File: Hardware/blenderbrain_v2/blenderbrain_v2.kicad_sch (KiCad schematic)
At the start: 49 parts, among them J1 OxySens2, J2 HeSens1, J24V1 Screw_Terminal_01x02, J3 HeSens2, J4 OxySens1, J5 Conn_01x04_Female, J5V1 Screw_Terminal_01x02, J6 AVR-ISP-6, Q1 IRFR4105, Q2 IRFR4105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

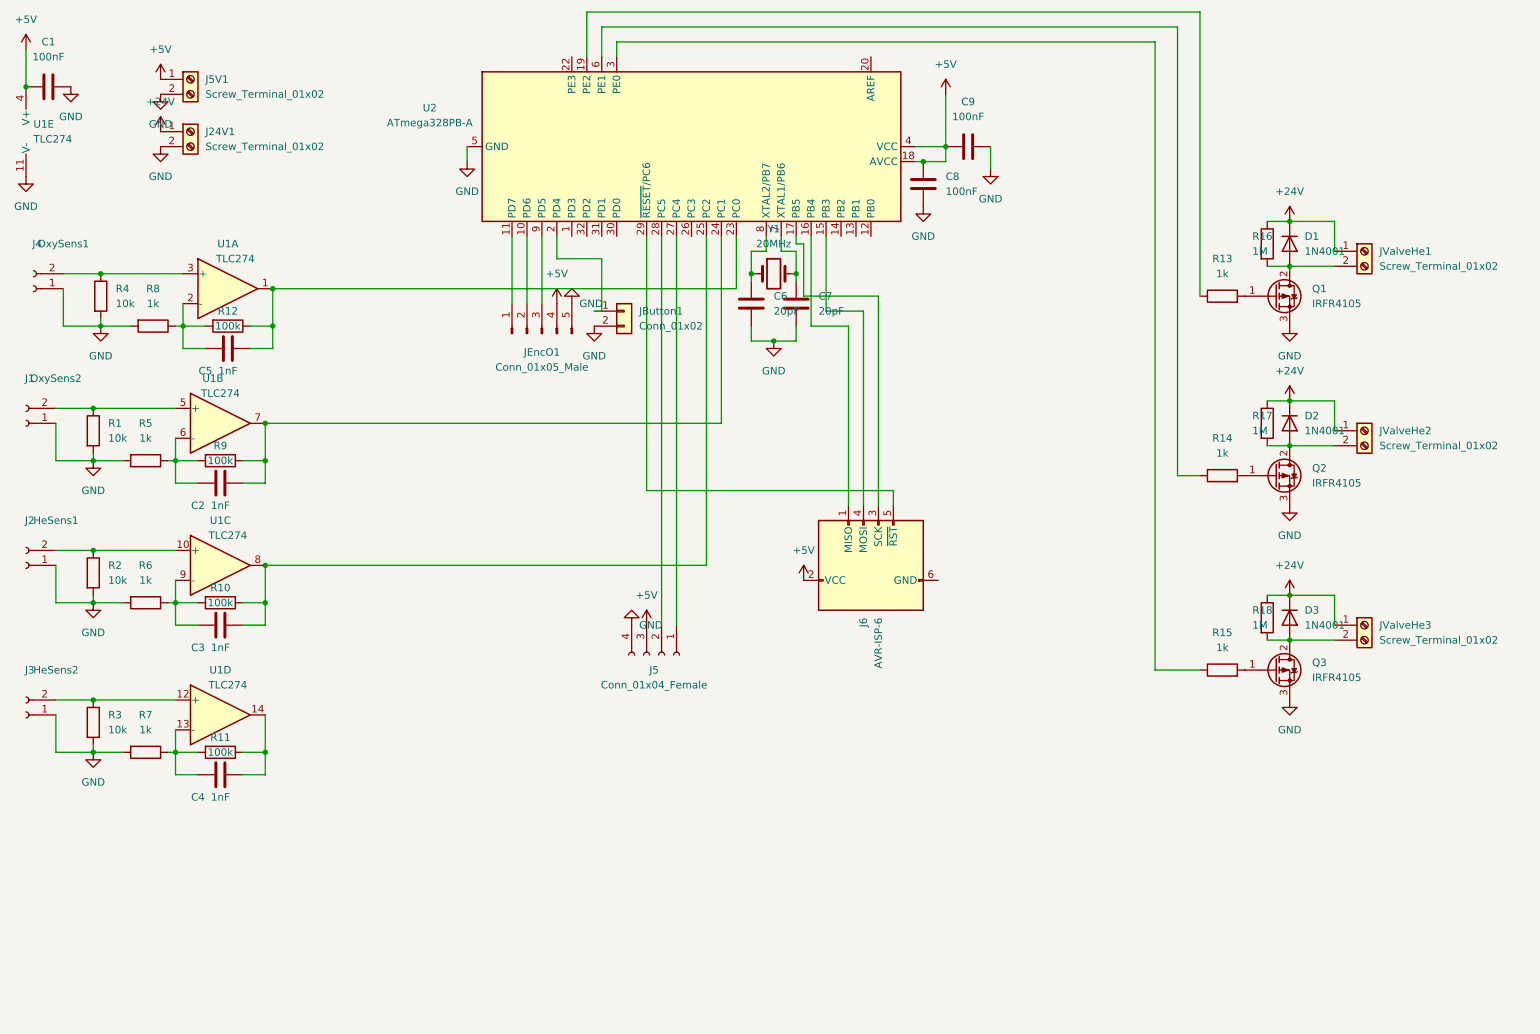
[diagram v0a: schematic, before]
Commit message: hardware: added rotary encoder to pcb and made first alignment
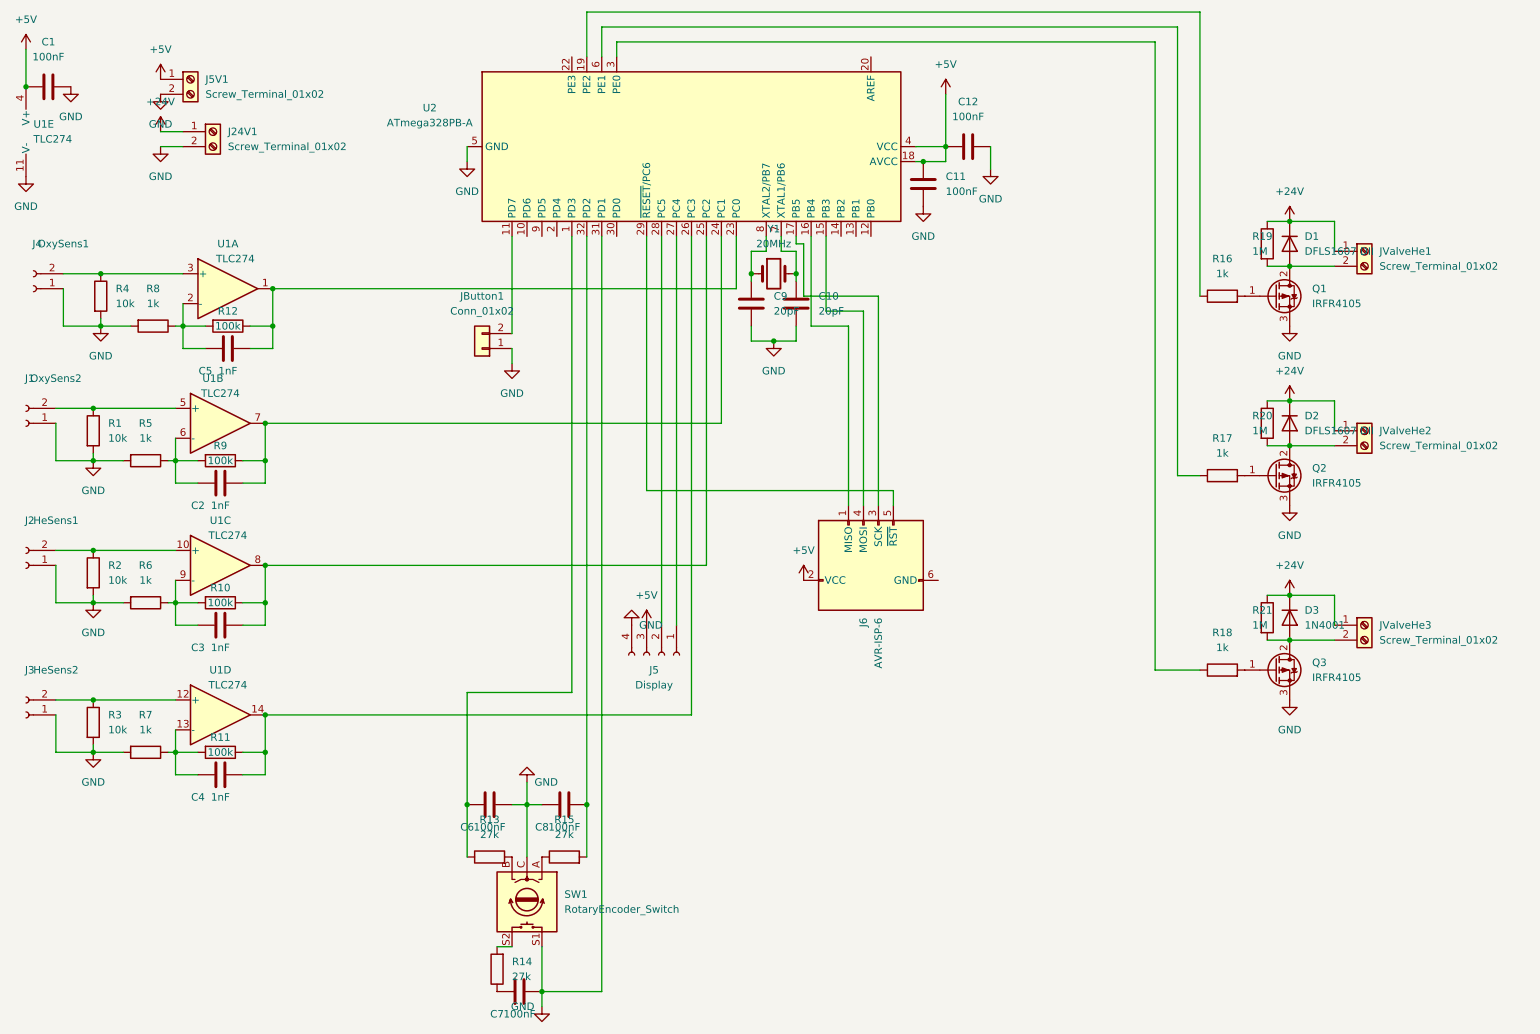
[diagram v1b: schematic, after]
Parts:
- removed JEncO1: Conn_01x05_Male, Connector_PinHeader_2.54mm:PinHeader_1x05_P2.54mm_Vertical, symbol Connector:Conn_01x05_Male
- added C6, C7, C8: 100nF, Capacitor_SMD:C_1206_3216Metric, symbol Device:C
- added R13, R14, R15: 27k, Resistor_SMD:R_1206_3216Metric, symbol Device:R
- added SW1: RotaryEncoder_Switch, Rotary_Encoder:RotaryEncoder_Alps_EC11E-Switch_Vertical_H20mm, symbol Device:RotaryEncoder_Switch
- C1, C2, C3, C4, C5: footprint Capacitor_THT:C_Disc_D4.3mm_W1.9mm_P5.00mm -> Capacitor_SMD:C_1206_3216Metric
- C10: renamed from C7; footprint Capacitor_THT:C_Disc_D4.3mm_W1.9mm_P5.00mm -> Capacitor_SMD:C_1206_3216Metric
- C11: renamed from C8; footprint Capacitor_THT:C_Disc_D4.3mm_W1.9mm_P5.00mm -> Capacitor_SMD:C_1206_3216Metric
- C12: renamed from C9; footprint Capacitor_THT:C_Disc_D4.3mm_W1.9mm_P5.00mm -> Capacitor_SMD:C_1206_3216Metric
- C9: renamed from C6; footprint Capacitor_THT:C_Disc_D4.3mm_W1.9mm_P5.00mm -> Capacitor_SMD:C_1206_3216Metric
- D1, D2: value 1N4001 -> DFLS1607 DII; footprint Diode_THT:D_DO-41_SOD81_P10.16mm_Horizontal -> Diode_SMD:D_PowerDI-123
- D3: footprint Diode_THT:D_DO-41_SOD81_P10.16mm_Horizontal -> Diode_SMD:D_PowerDI-123
- J1, J2, J3, J4: footprint (none) -> Connector_JST:JST_EH_S2B-EH_1x02_P2.50mm_Horizontal
- J5: value Conn_01x04_Female -> Display; footprint (none) -> Connector_PinSocket_2.54mm:PinSocket_1x04_P2.54mm_Vertical
- JValveHe1, JValveHe2, JValveHe3: footprint TerminalBlock:TerminalBlock_bornier-2_P5.08mm -> Connector_JST:JST_EH_B2B-EH-A_1x02_P2.50mm_Vertical
- R1, R10, R11, R12, R2, R3, R4, R5, R6, R7, R8, R9: footprint Resistor_THT:R_Axial_DIN0204_L3.6mm_D1.6mm_P7.62mm_Horizontal -> Resistor_SMD:R_1206_3216Metric
- R16: renamed from R13; footprint (none) -> Resistor_SMD:R_1206_3216Metric
- R17: renamed from R14; footprint (none) -> Resistor_SMD:R_1206_3216Metric
- R18: renamed from R15; footprint (none) -> Resistor_SMD:R_1206_3216Metric
- R19: renamed from R16; footprint (none) -> Resistor_SMD:R_1206_3216Metric
- R20: renamed from R17; footprint (none) -> Resistor_SMD:R_1206_3216Metric
- R21: renamed from R18; footprint (none) -> Resistor_SMD:R_1206_3216Metric
- U1: footprint (none) -> Package_SO:SO-14_3.9x8.65mm_P1.27mm
- Y1: footprint Crystal:Resonator-2Pin_W7.0mm_H2.5mm -> Crystal:Crystal_HC49-U_Vertical
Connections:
- net GND: now also JButton1.1 (Pin_1), U2.31 (PD1), C6.2, C7.2, C8.1, SW1.C, SW1.S1; no longer JButton1.2 (Pin_2)
- net at U2.1 (PD3): now also C6.1, R13.1
- net at U2.11 (PD7): now also JButton1.2 (Pin_2)
- net at U2.2 (PD4): no longer JButton1.1 (Pin_1)
- net at U2.26 (PC3): now also C4.2, R11.1, U1.14
- net at U2.32 (PD2): now also C8.2, R15.2
- new net: C7.1, R14.1
- new net: R14.2, SW1.S2
- new net: R15.1, SW1.A
- new net: R13.2, SW1.B
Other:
- moved on the sheet: J24V1, JButton1
